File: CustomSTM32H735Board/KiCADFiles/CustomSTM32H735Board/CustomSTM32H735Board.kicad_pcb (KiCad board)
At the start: 4 copper layers, 127 x 73 mm, 99 parts, among them IC1 NCP700BSN33T1G, J1 FLE-125-01-G-DV, SW1 SW_Omron_B3FS, U1 L7805, U2 OPA1678IDGKT, U3 STM32H735IGT6, X1 NSC5004A-25M

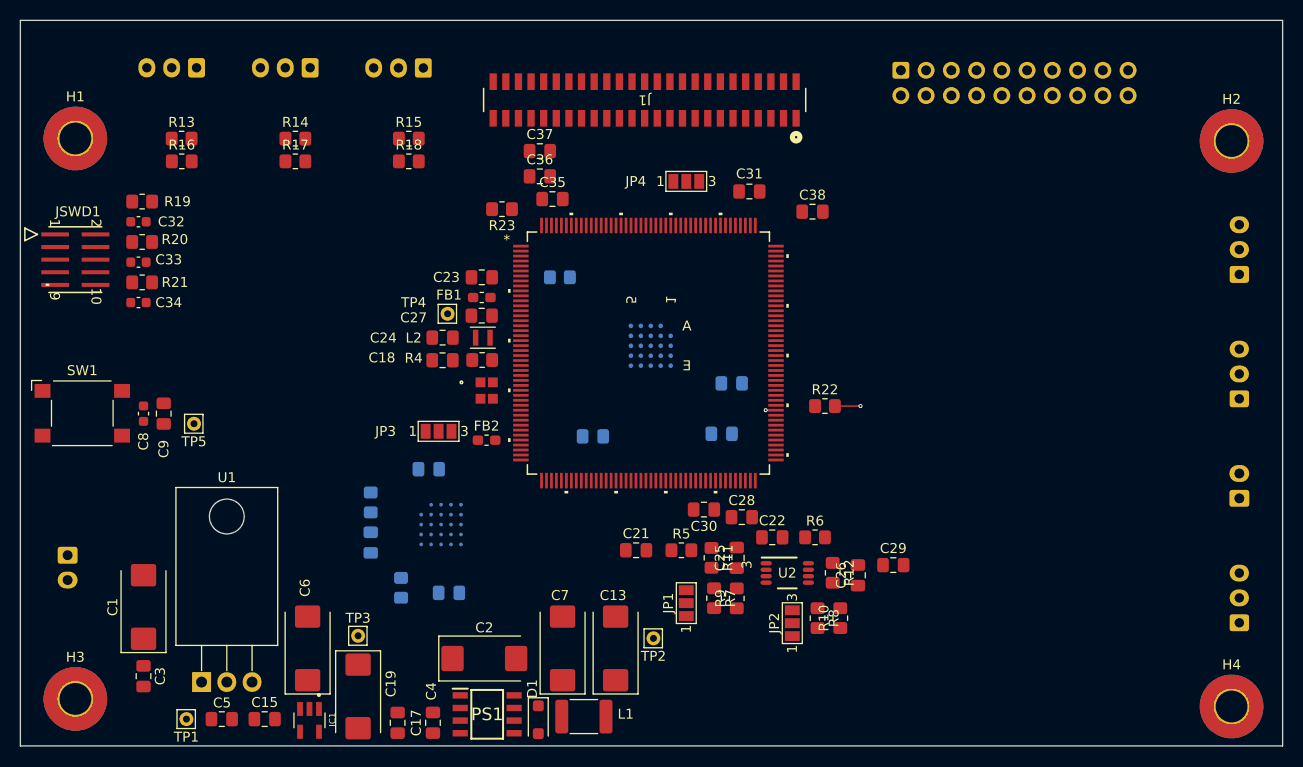
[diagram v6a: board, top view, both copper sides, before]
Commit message: work on layout, first possible solution
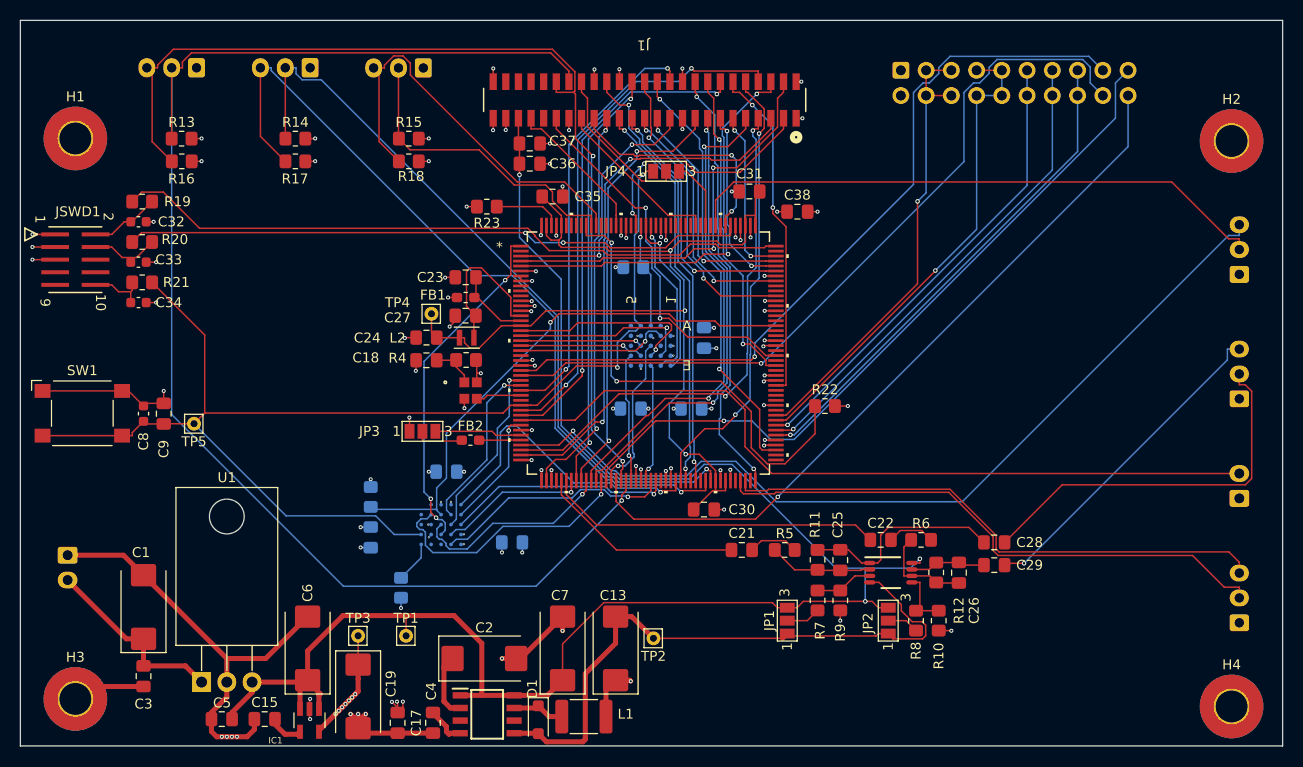
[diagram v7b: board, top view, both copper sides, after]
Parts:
- moved C28 25.5 mm to (158.0, 112.5)
- moved TP1 23.6 mm to (98.8, 121.9)
- moved C22 10.9 mm to (146.6, 112.3)
- moved R6 10.7 mm to (150.6, 112.3)
- moved R11 10.7 mm to (140.2, 114.3)
- moved C21 10.6 mm to (132.6, 113.3)
- moved C25 10.4 mm to (142.5, 114.3)
- moved R7 10.4 mm to (140.2, 118.4)
- moved R9 10.4 mm to (142.5, 118.4)
- moved U2 10.4 mm to (147.6, 115.6)
- moved R12 10.4 mm to (152.1, 115.6)
- moved R5 10.4 mm to (136.9, 113.3)
- moved JP1 10.3 mm to (137.2, 120.4)
- moved C26 10.2 mm to (154.4, 115.6)
- moved C29 10.2 mm to (158.0, 114.8)
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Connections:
- U3 pad 14: /VSSSMPS -> GND
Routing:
- net +5V: track 0.00 -> 178.1 mm, vias 0 -> 3
- net GND: track 2.57 -> 171.8 mm, vias 1 -> 75
- net /PF15: track 0.00 -> 143.0 mm, vias 0 -> 1
- net /NRST: track 0.00 -> 126.6 mm, vias 0 -> 2
- net /PF14: track 0.00 -> 101.4 mm, vias 0 -> 2
- net /VDD_SDC: track 0.00 -> 98.3 mm, vias 0 -> 3
- net /PA0: track 0.00 -> 89.3 mm, vias 0 -> 1
- net /PB10: track 0.00 -> 80.7 mm, vias 0 -> 1
- net /PC2_C: track 0.00 -> 79.2 mm
- net /PF6: track 0.00 -> 78.8 mm, vias 0 -> 1
- net /PF7: track 0.00 -> 78.6 mm, vias 0 -> 1
- net /PB11: track 0.00 -> 75.6 mm, vias 0 -> 1
- net /PF13: track 0.00 -> 75.0 mm, vias 0 -> 1
- net /PF11: track 0.00 -> 73.8 mm, vias 0 -> 1
- net /PA13: track 0.00 -> 68.5 mm
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
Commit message: finished PCB and ordered at AISLER
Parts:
- renumbered JADC1 to JADC, JDAC1 to JDAC, JI2C3 to JI2C, JI2C1 to JI2C, JI2C2 to JI2C, J1 to JLCD, JPOWER1 to JPOWER, JSWD1 to JSWD, JUART1 to JUART, SW1 to SW
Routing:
- net +3.3V: track 66.2 -> 74.9 mm, vias 52 -> 56
- net GND: track 171.8 -> 174.7 mm, vias 75 -> 78
- added copper zone on B.Cu, net GND
- added copper zone on F.Cu, net GND
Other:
- board text added: "Stefan Meyre, HB9GZE, CPU rev. 1.0"
